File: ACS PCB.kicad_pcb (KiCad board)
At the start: 4 copper layers, 72.4 x 72.4 mm, 64 parts, among them J1 Conn_01x02, J3 Conn_01x01, J5 Conn_01x02, Q1 2SC1815, U1 LSM6DSV80XTR, U3 LSM6DSV80XTR, U4 BMP581, U5 BMP581, U6 BMP581, U7 LSM6DSV80XTR, U8 PLM62440APPQRJRTQ1

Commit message: Added standoff hole
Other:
- outline, holes or cut-outs redrawn

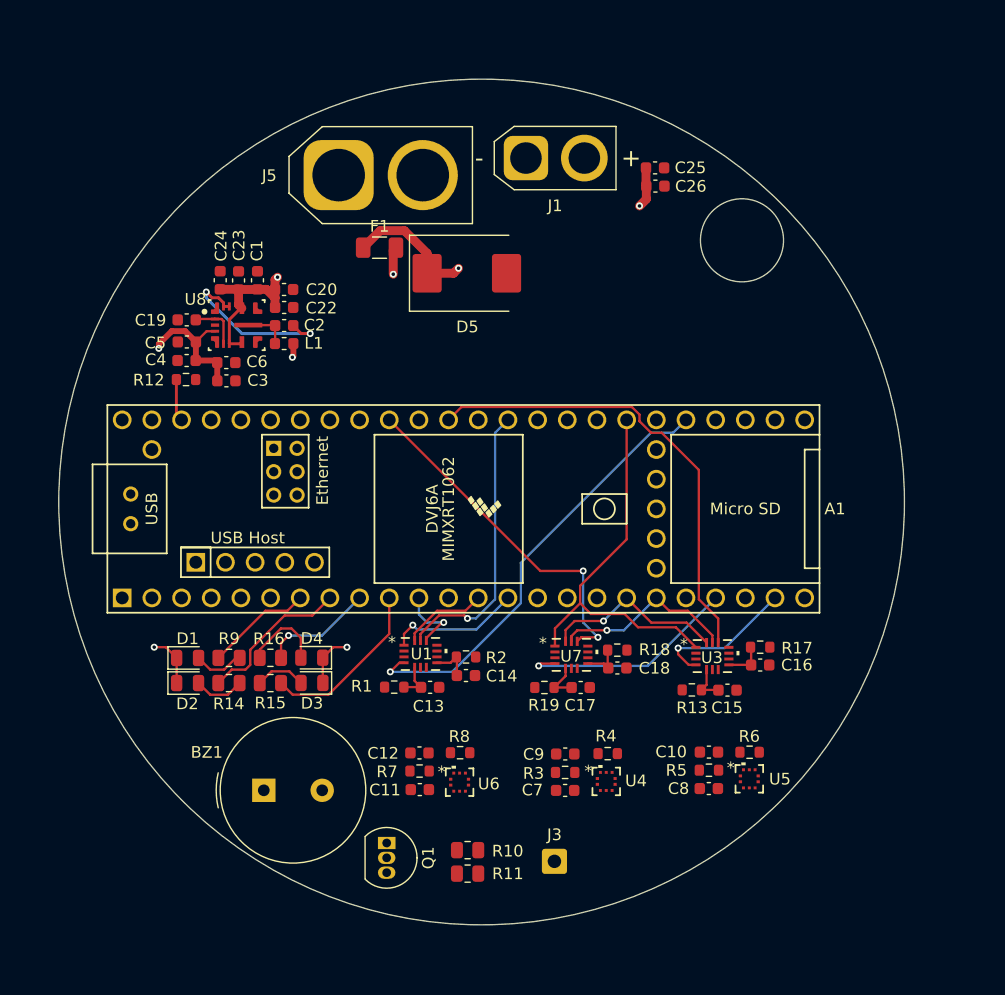
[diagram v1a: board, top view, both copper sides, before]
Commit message: Added all standoff holes
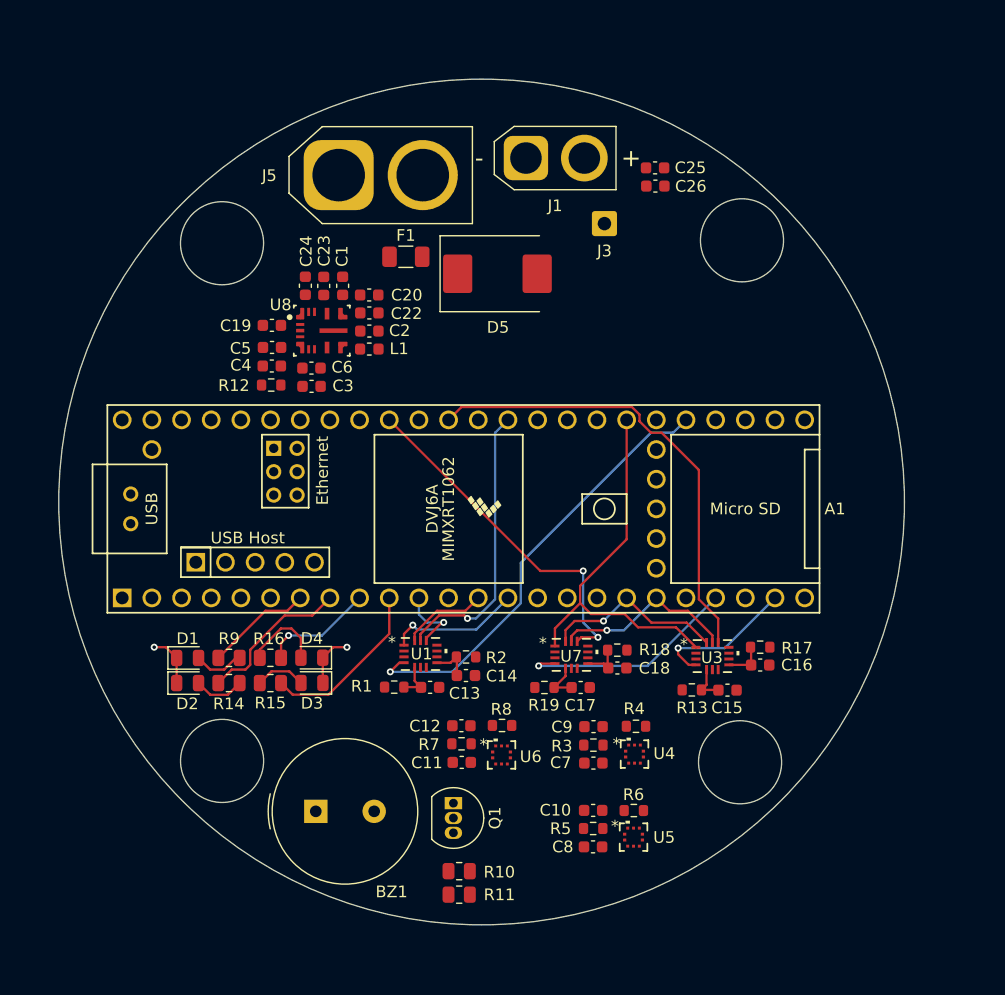
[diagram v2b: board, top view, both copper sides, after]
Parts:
- moved J3 54.8 mm to (158.5, 63.7)
- moved C10 11.1 mm to (157.6, 114.0)
- moved R5 11.1 mm to (157.6, 115.5)
- moved C8 11.1 mm to (157.6, 117.1)
- moved R6 11.1 mm to (161.1, 114.0)
- moved U5 11.1 mm to (161.0, 116.3)
- moved R12 7.31 mm to (130.0, 77.6)
- moved C3 7.31 mm to (133.5, 77.7)
- moved C5 7.31 mm to (130.1, 74.3)
- moved C6 7.31 mm to (133.5, 76.1)
- moved C1 7.31 mm to (136.1, 69.1)
- moved C19 7.31 mm to (130.1, 72.4)
- moved C2 7.31 mm to (138.4, 72.9)
- moved C20 7.31 mm to (138.4, 69.8)
- moved C22 7.31 mm to (138.4, 71.4)
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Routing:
- net +BATT: track 73.4 -> 0.00 mm, vias 3 -> 0
- net +5V: track 31.6 -> 0.00 mm, vias 2 -> 0
- net Net-(U8-CBOOT): track 15.1 -> 0.00 mm, vias 2 -> 0
- net Net-(U8-MODE_SYNC): track 4.60 -> 0.00 mm
- net Net-(U8-SW): track 3.86 -> 0.00 mm
- net +3.3V: track 3.63 -> 0.00 mm
- net Net-(J5-Pin_1): track 14.8 -> 12.4 mm, vias 1 -> 0
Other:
- outline, holes or cut-outs redrawn

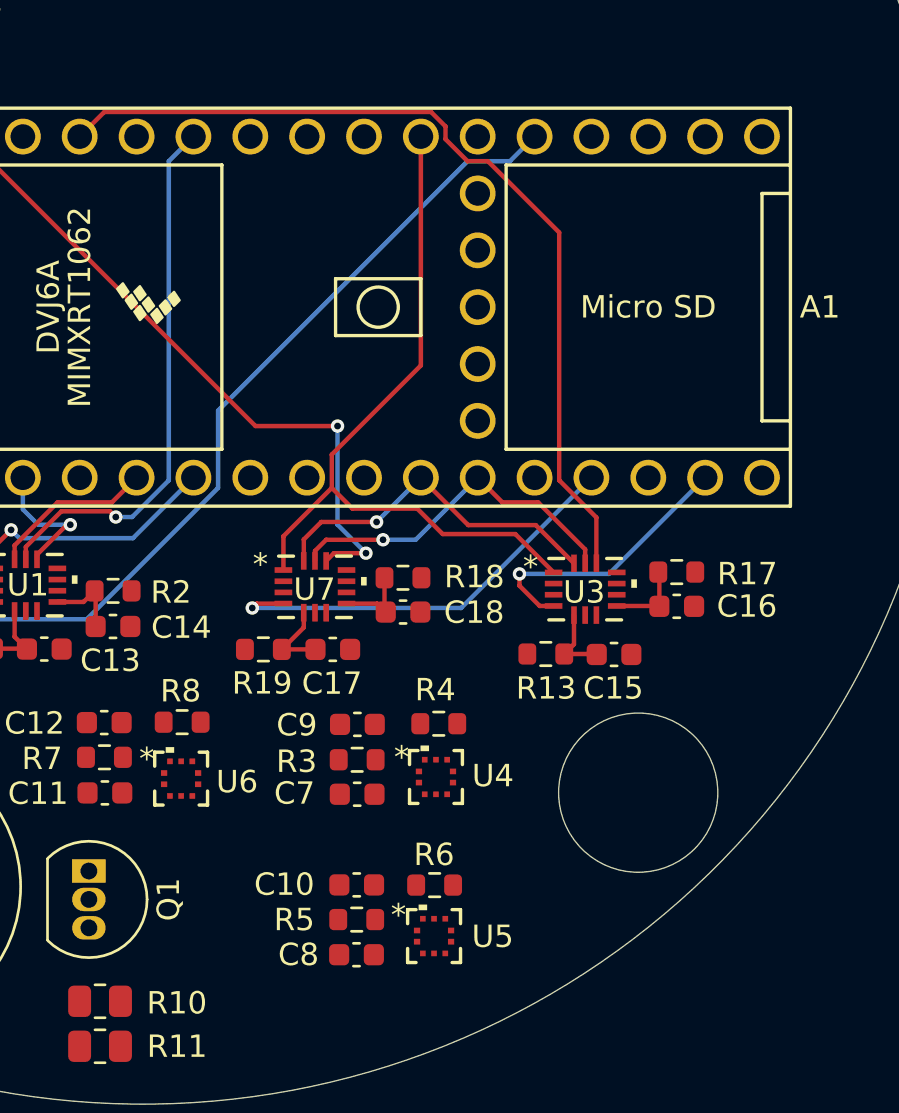
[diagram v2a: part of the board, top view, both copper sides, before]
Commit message: routed U5, altimeter
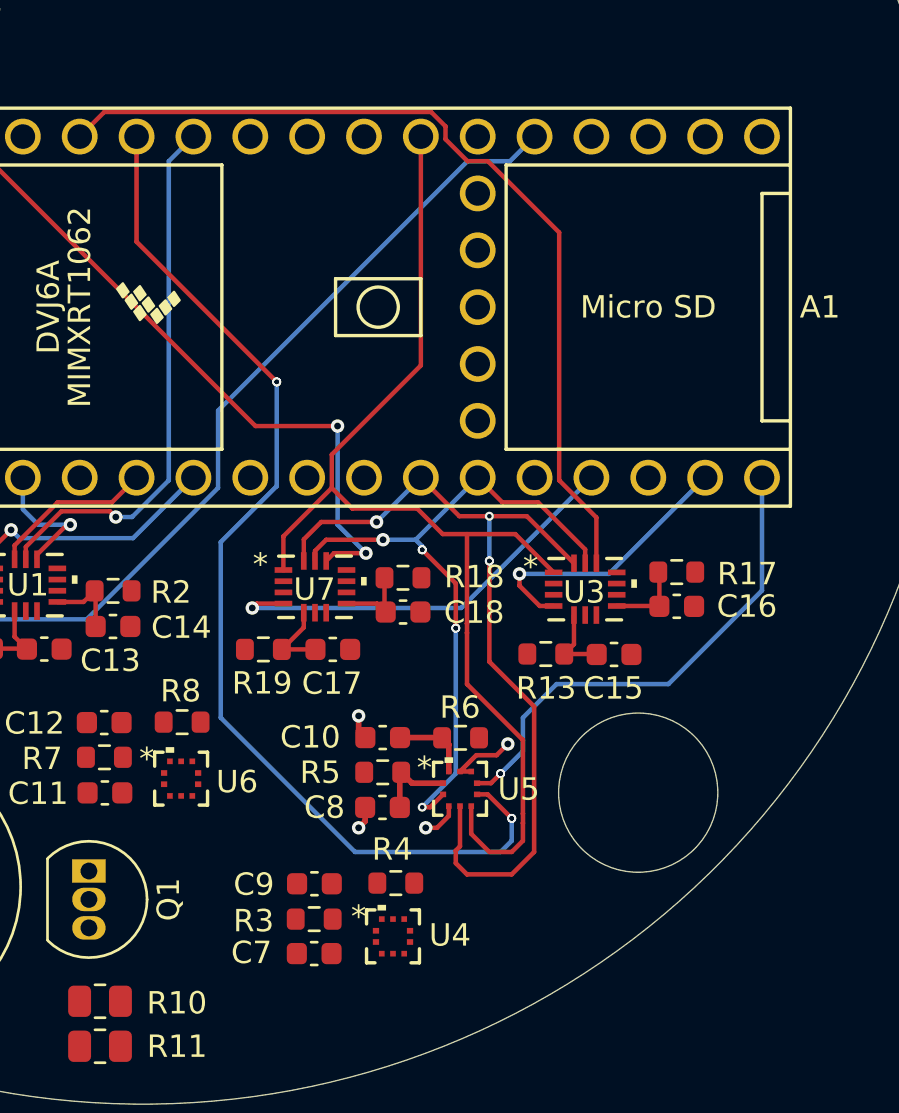
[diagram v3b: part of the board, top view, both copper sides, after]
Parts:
- moved R4 7.37 mm to (159.3, 113.9)
- moved C7 7.37 mm to (155.7, 117.0)
- moved C9 7.37 mm to (155.7, 113.9)
- moved R3 7.37 mm to (155.7, 115.5)
- moved U4 7.37 mm to (159.2, 116.3)
- moved C10 6.68 mm to (158.7, 107.4)
- moved R5 6.68 mm to (158.7, 108.9)
- moved C8 6.68 mm to (158.7, 110.5)
- moved R6 6.68 mm to (162.2, 107.4)
- moved U5 6.68 mm to (162.2, 109.7)
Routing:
- net CS_A1: track 0.00 -> 48.3 mm, vias 0 -> 4
- net MOSI1: track 15.8 -> 38.3 mm, vias 1 -> 4
- net INT_A1: track 0.00 -> 22.3 mm, vias 0 -> 2
- net MISO1: track 33.4 -> 52.2 mm
- net SCK1: track 15.8 -> 30.4 mm, vias 1 -> 6
- net GND: track 9.09 -> 16.0 mm, vias 2 -> 6
- net Net-(U5-VDDIO): track 0.00 -> 3.67 mm
- net Net-(U5-VDD): track 0.00 -> 3.51 mm

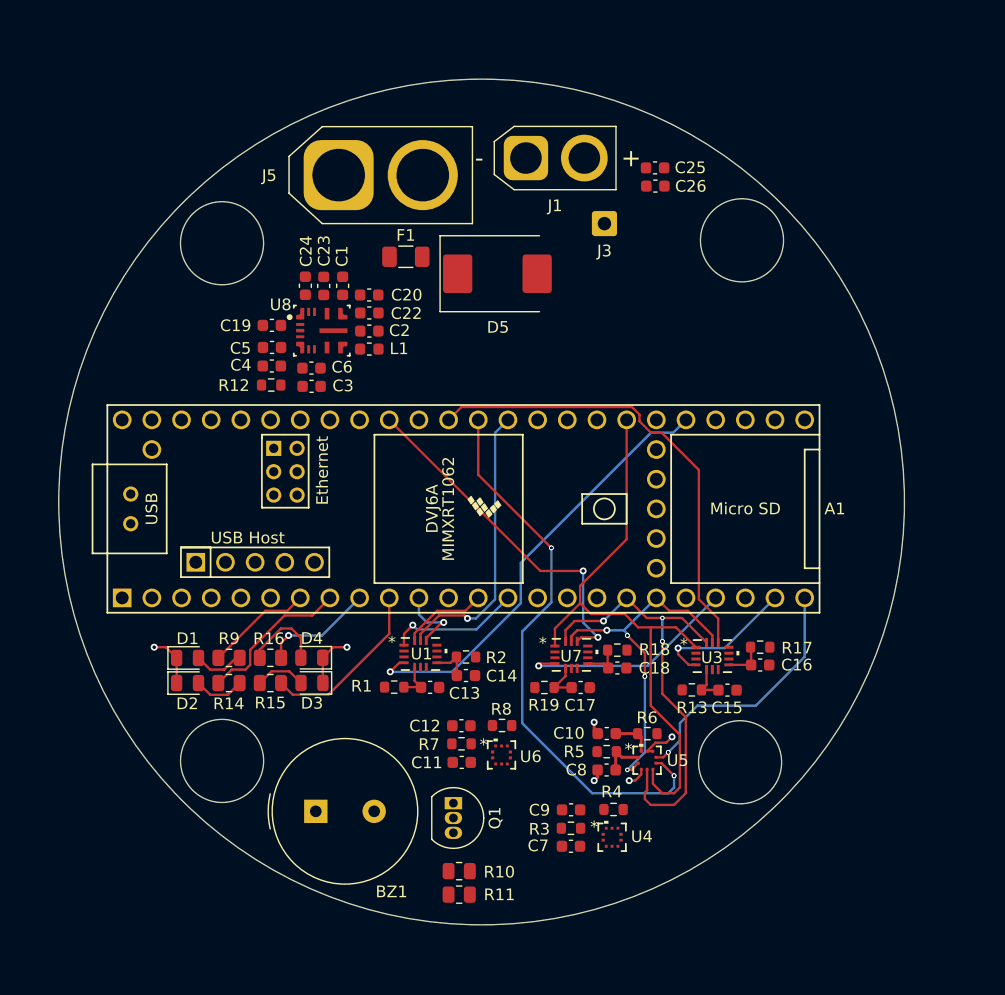
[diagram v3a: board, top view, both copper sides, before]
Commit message: Wired LM62440 and GNDs/3.3Vs
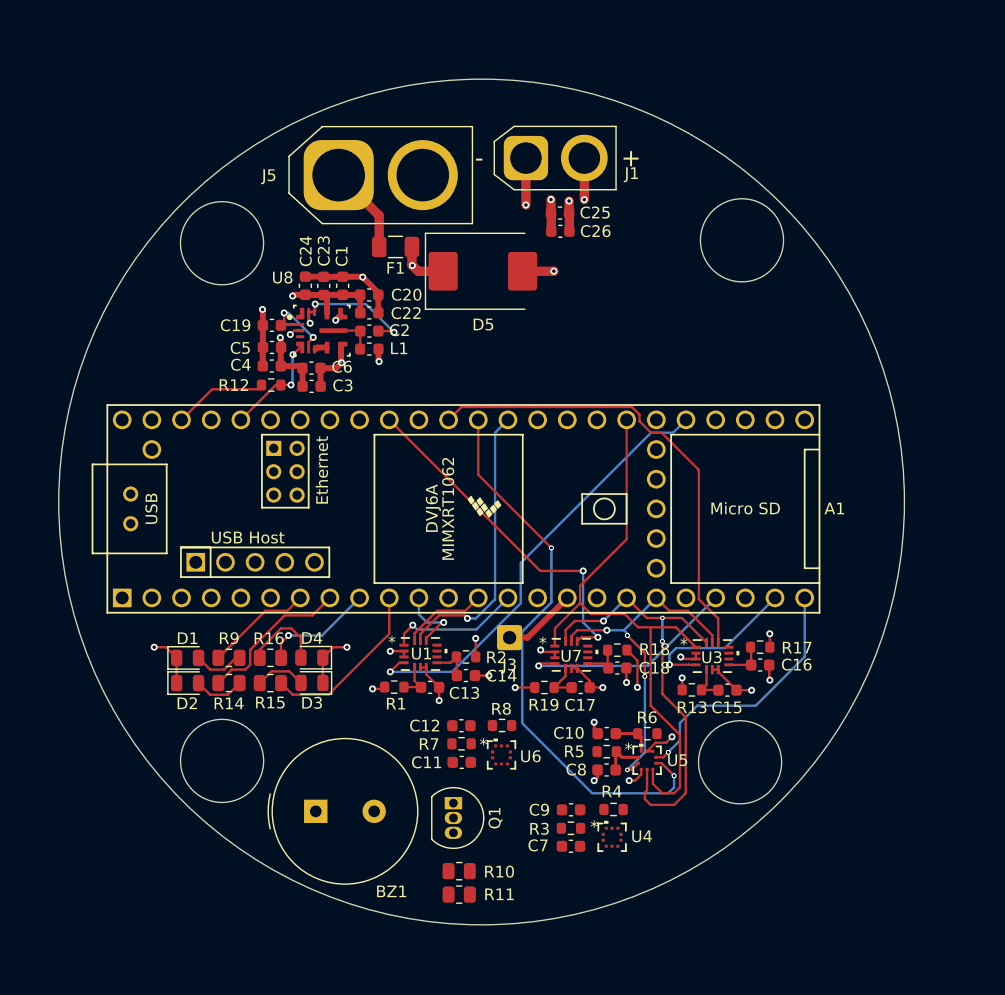
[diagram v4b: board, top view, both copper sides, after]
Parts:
- moved J3 36.4 mm to (150.4, 99.2)
- moved C26 9.01 mm to (154.8, 64.4)
- moved C25 9.01 mm to (154.7, 62.8)
- moved D5 1.27 mm to (148.1, 67.8)
- moved F1 1.22 mm to (140.7, 65.7), turned to 180 degrees
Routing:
- net GND: track 16.0 -> 67.2 mm, vias 6 -> 23
- net +BATT: track 0.00 -> 21.3 mm, vias 0 -> 4
- net +3.3V: track 0.00 -> 18.4 mm, vias 0 -> 6
- net Net-(U8-CBOOT): track 0.00 -> 11.4 mm, vias 0 -> 3
- net VoltMonitor: track 0.00 -> 9.57 mm, vias 0 -> 2
- net Net-(U8-MODE_SYNC): track 0.00 -> 7.38 mm, vias 0 -> 2
- net +5V: track 0.00 -> 7.04 mm, vias 0 -> 2
- net PWM_fs: track 0.00 -> 6.35 mm
- net Net-(J5-Pin_1): track 12.4 -> 7.59 mm
- net Net-(U8-SW): track 0.00 -> 3.86 mm
- net INT_I1: track 12.5 -> 14.2 mm
- added copper zone on In2.Cu, net +BATT
- removed copper zone on In2.Cu, net (none)

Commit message: Added mounting holes AGAIN UGH
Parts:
- added REF**: MountingHole_6.4mm_M6, MountingHole:MountingHole_6.4mm_M6, F.Cu at (172.6, 62.9)
- added REF**: MountingHole_6.4mm_M6, MountingHole:MountingHole_6.4mm_M6, F.Cu at (123.6, 112.1)
- added REF**: MountingHole_6.4mm_M6, MountingHole:MountingHole_6.4mm_M6, F.Cu at (123.6, 63.1)
- added REF**: MountingHole_6.4mm_M6, MountingHole:MountingHole_6.4mm_M6, F.Cu at (172.3, 112.1)
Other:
- outline, holes or cut-outs redrawn

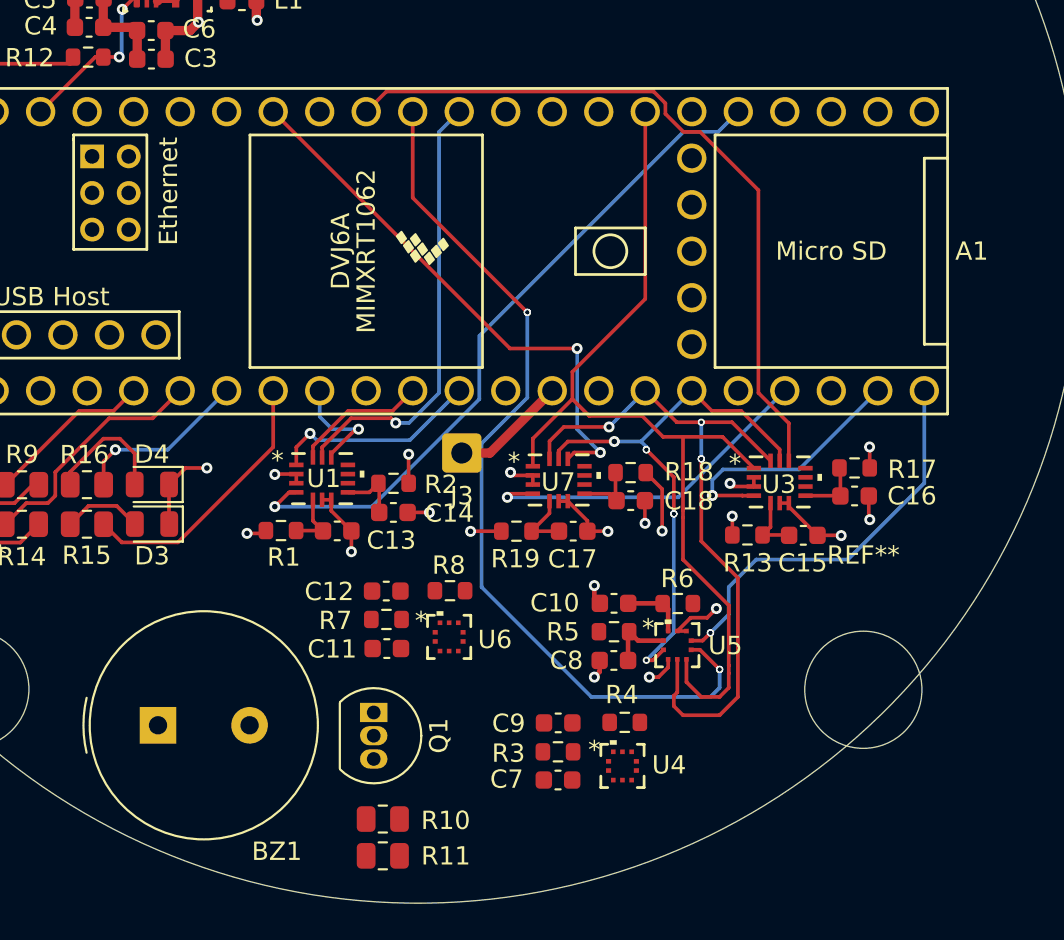
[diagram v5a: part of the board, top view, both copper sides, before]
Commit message: finished routing, except SCK0, couldnt find good path.
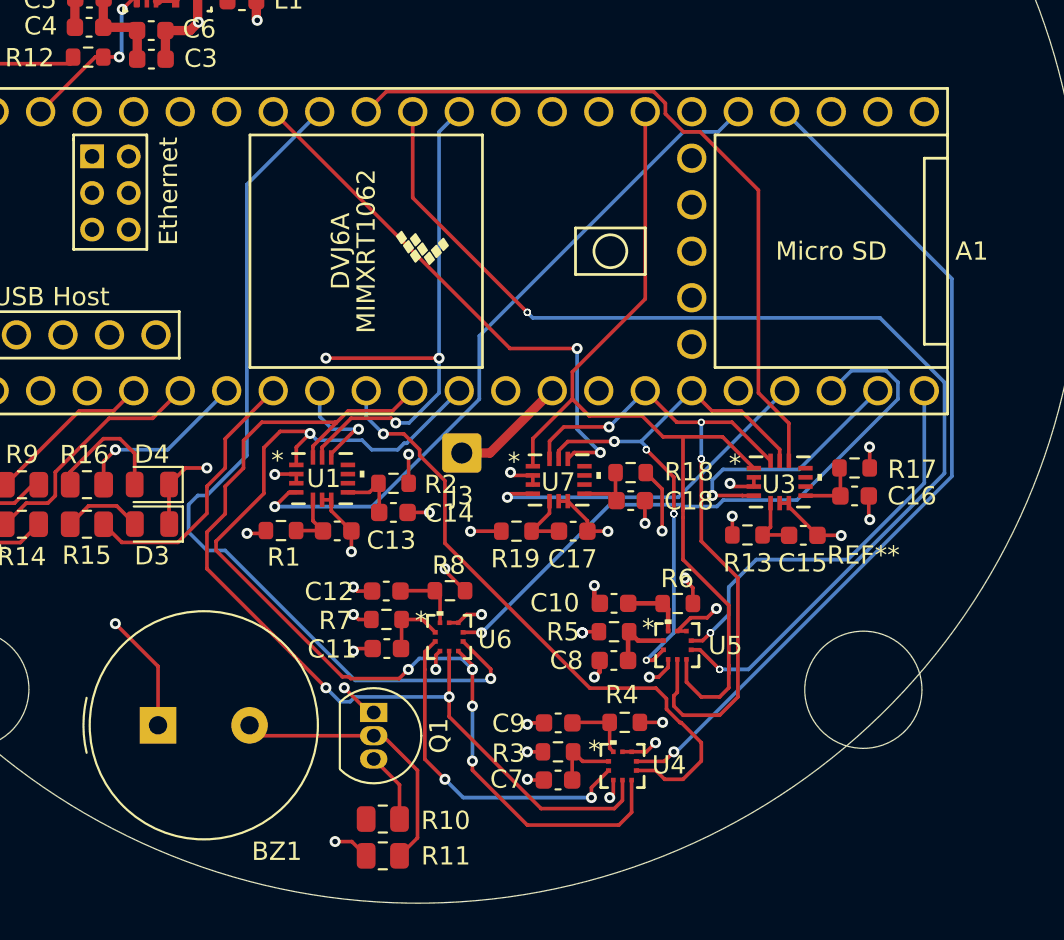
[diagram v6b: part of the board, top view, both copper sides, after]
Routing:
- net CS_A2: track 0.00 -> 48.8 mm, vias 0 -> 1
- net INT_A0: track 0.00 -> 47.4 mm, vias 0 -> 1
- net MISO0: track 11.4 -> 57.9 mm, vias 1 -> 5
- net MOSI0: track 7.32 -> 53.2 mm, vias 0 -> 2
- net CS_A0: track 0.00 -> 34.8 mm, vias 0 -> 1
- net INT_A2: track 0.00 -> 34.4 mm, vias 0 -> 1
- net SCK0: track 24.2 -> 49.1 mm, vias 1 -> 5
- net Net-(BZ1--): track 0.00 -> 15.3 mm
- net CS_A1: track 48.3 -> 61.6 mm
- net GND: track 67.2 -> 79.6 mm, vias 23 -> 32
- net 3.3V: track 0.00 -> 8.53 mm, vias 0 -> 2
- net +3.3V: track 18.4 -> 25.7 mm, vias 6 -> 13
- net Net-(Q1-B): track 0.00 -> 3.86 mm
- net Net-(U6-VDD): track 0.00 -> 3.75 mm
- net Net-(U4-VDD): track 0.00 -> 3.74 mm
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
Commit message: Finished up PCB [DRAFT]
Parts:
- removed the REF** at (123.6, 112.1)
- removed the REF** at (123.6, 63.1)
- removed the REF** at (172.3, 112.1)
- added ?: , , F.Cu at (173.6, 113.2)
- added ?: , , F.Cu at (122.4, 62.0)
- added ?: , , F.Cu at (173.6, 62.0)
- added ?: , , F.Cu at (122.4, 113.2)
- added ?: , , F.Cu at (123.8, 111.8)
- added ?: , , F.Cu at (123.8, 63.4)
- added ?: , , F.Cu at (172.2, 111.8)
- L1: value 4.7uH -> 1090_78439369047; footprint Inductor_SMD:L_0603_1608Metric -> Inductor78439358047:L_Wurth_WE-XHMA-1090
- moved D5 12.7 mm to (160.8, 69.0)
- moved L1 10.3 mm to (148.6, 73.2)
- moved C1 8.55 mm to (135.6, 77.6), turned to 0 degrees
- moved C23 7.84 mm to (133.2, 76.8), turned to -90 degrees
- moved C24 7.44 mm to (135.6, 76.0), turned to 0 degrees
- moved C2 6.42 mm to (133.2, 69.2), turned to -90 degrees
- moved C3 5.92 mm to (138.4, 74.4)
- moved C6 5.92 mm to (138.4, 72.8)
- moved C26 1.89 mm to (156.7, 64.3)
- moved J1 1.89 mm to (153.7, 58.0)
- moved C25 1.89 mm to (156.6, 62.7)
- moved REF** 0.65 mm to (172.2, 63.4)
- moved BZ1 0.40 mm to (134.2, 114.0)
- moved C20 0.19 mm to (138.4, 69.7)
- moved C22 0.19 mm to (138.4, 71.2)
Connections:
- A1 pad 23: unconnected-(A1-A9-Pad23) -> Buzzer
- A1 pad 33: Buzzer -> unconnected-(A1-D33-Pad33)
- BZ1 pad 1: 3.3V -> +3.3V
- R11 pad 1: 3.3V -> +3.3V
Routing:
- net Buzzer: track 0.00 -> 49.0 mm, vias 0 -> 1
- net Net-(U8-SW): track 3.86 -> 21.8 mm, vias 0 -> 2
- net +5V: track 7.04 -> 24.9 mm, vias 2 -> 4
- net SCK0: track 49.1 -> 62.4 mm, vias 5 -> 6
- net Net-(U8-CBOOT): track 11.4 -> 2.04 mm, vias 3 -> 0
- net +3.3V: track 25.7 -> 34.7 mm, vias 13 -> 14
- net 3.3V: track 8.53 -> 0.00 mm, vias 2 -> 0
- net +BATT: track 21.3 -> 27.1 mm, vias 4 -> 7
- net GND: track 79.6 -> 82.8 mm, vias 32 -> 36
- net Net-(U8-MODE_SYNC): track 7.38 -> 4.38 mm, vias 2 -> 0
- net VoltMonitor: track 9.57 -> 8.85 mm, vias 2 -> 0
- net MOSI1: track 38.3 -> 38.8 mm, vias 4 -> 3
- net SCK1: track 30.4 -> 30.5 mm, vias 6 -> 4
- net INT_A1: vias 2 -> 1
- net CS_A1: vias 4 -> 2
- removed copper zone on In2.Cu, net GND
